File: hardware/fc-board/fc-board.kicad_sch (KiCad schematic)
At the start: 0 parts

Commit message: Add hierarchical sheet structure: power, MCU, IMU, motors, radio
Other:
- added sheet IMU (imu.kicad_sch)
- added sheet MCU (mcu.kicad_sch)
- added sheet Motors (motors.kicad_sch)
- added sheet Power (power.kicad_sch)
- added sheet Radio (radio.kicad_sch)
- company: (none) -> Brody Barrett
- title: (none) -> STM32 Quadcopter Flight Controller
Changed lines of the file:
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@@
 	(generator_version "10.0")
 	(paper "A4")
+	(title_block
+		(title "STM32 Quadcopter Flight Controller")
+		(company "Brody Barrett")
+		(comment 1 "Rev A")
+		(comment 2 "github.com/barrettbrody06/stm32-quadcopter-fc")
+	)
+	(sheet
+		(at 190.5 16.51)
+		(size 87.63 62.23)
+		(exclude_from_sim no)
+		(in_bom yes)
+		(on_board yes)
+		(dnp no)
+		(fields_autoplaced yes)
+		(stroke
+			(width 0.1524)
+			(type solid)
+		)
+		(fill
+			(color 0 0 0 0)
+		)
+		(property "Sheetname" "Radio"
+			(at 190.5 15.7984 0)
+			(show_name no)
+			(do_not_autoplace no)
+			(effects
+				(font
+					(size 1.27 1.27)
+				)
+				(justify left bottom)
+			)
+		)
+		(property "Sheetfile" "radio.kicad_sch"
+			(at 190.5 79.3246 0)
+			(show_name no)
+			(do_not_autoplace no)
+			(effects
+				(font
+					(size 1.27 1.27)
+				)
+				(justify left top)
+			)
+		)
+		(instances
+			(project "fc-board"
+				(path "/953cb3c2-4b9e-42b9-907c-fb15c6a3ba2f"
+					(page "6")
+				)
+			)
+		)
+	)
+	(sheet
+		(at 97.79 16.51)
+		(size 86.36 109.22)
+		(exclude_from_sim no)
+		(in_bom yes)
+		(on_board yes)
+		(dnp no)
+		(fields_autoplaced yes)
+		(stroke
+			(width 0.1524)
+			(type solid)
+		)
+		(fill
+			(color 0 0 0 0)
+		)
+		(property "Sheetname" "MCU"
+			(at 97.79 15.7984 0)
+			(show_name no)
+			(do_not_autoplace no)
+			(effects
+				(font
+					(size 1.27 1.27)
+				)
+				(justify left bottom)
+			)
+		)
+		(property "Sheetfile" "mcu.kicad_sch"
+			(at 97.79 126.3146 0)
+			(show_name no)
+			(do_not_autoplace no)
+			(effects
+				(font
+					(size 1.27 1.27)
+				)
+				(justify left top)
+			)
+		)
+		(instances
+			(project "fc-board"
+				(path "/953cb3c2-4b9e-42b9-907c-fb15c6a3ba2f"
+					(page "3")
+				)
+			)
+		)
+	)
+	(sheet
+		(at 15.24 16.51)
+		(size 74.93 40.64)
+		(exclude_from_sim no)
+		(in_bom yes)
+		(on_board yes)
+		(dnp no)
+		(fields_autoplaced yes)
+		(stroke
+			(width 0.1524)
+			(type solid)
+		)
+		(fill
+			(color 0 0 0 0)
+		)
+		(property "Sheetname" "Power"
+			(at 15.24 15.7984 0)
+			(show_name no)
+			(do_not_autoplace no)
+			(effects
+				(font
+					(size 1.27 1.27)
+				)
+				(justify left bottom)
+			)
+		)
+		(property "Sheetfile" "power.kicad_sch"
+			(at 15.24 57.7346 0)
+			(show_name no)
+			(do_not_autoplace no)
+			(effects
+				(font
+					(size 1.27 1.27)
+				)
+				(justify left top)
+			)
+		)
+		(instances
+			(project "fc-board"
+				(path "/953cb3c2-4b9e-42b9-907c-fb15c6a3ba2f"
+					(page "2")
+				)
+			)
+		)
+	)
+	(sheet
+		(at 83.82 132.08)
+		(size 90.17 63.5)
+		(exclude_from_sim no)
+		(in_bom yes)
+		(on_board yes)
+		(dnp no)
+		(fields_autoplaced yes)
+		(stroke
+			(width 0.1524)
+			(type solid)
+		)
+		(fill
+			(color 0 0 0 0)
+		)
+		(property "Sheetname" "Motors"
+			(at 83.82 131.3684 0)
+			(show_name no)
+			(do_not_autoplace no)
+			(effects
+				(font
+					(size 1.27 1.27)
+				)
+				(justify left bottom)
+			)
+		)
+		(property "Sheetfile" "motors.kicad_sch"
+			(at 83.82 196.1646 0)
+			(show_name no)
+			(do_not_autoplace no)
+			(effects
+				(font
+					(size 1.27 1.27)
+				)
+				(justify left top)
+			)
+		)
+		(instances
+			(project "fc-board"
+				(path "/953cb3c2-4b9e-42b9-907c-fb15c6a3ba2f"
+					(page "5")
+				)
+			)
+		)
+	)
+	(sheet
+		(at 15.24 68.58)
+		(size 74.93 57.15)
+		(exclude_from_sim no)
+		(in_bom yes)
+		(on_board yes)
+		(dnp no)
+		(fields_autoplaced yes)
+		(stroke
+			(width 0.1524)
+			(type solid)
+		)
+		(fill
+			(color 0 0 0 0)
+		)
+		(property "Sheetname" "IMU"
+			(at 15.24 67.8684 0)
+			(show_name no)
+			(do_not_autoplace no)
+			(effects
+				(font
+					(size 1.27 1.27)
+				)
+				(justify left bottom)
+			)
+		)
+		(property "Sheetfile" "imu.kicad_sch"
+			(at 15.24 126.3146 0)
+			(show_name no)
+			(do_not_autoplace no)
+			(effects
+				(font
+					(size 1.27 1.27)
+				)
+				(justify left top)
+			)
+		)
+		(instances
+			(project "fc-board"
+				(path "/953cb3c2-4b9e-42b9-907c-fb15c6a3ba2f"
+					(page "4")
+				)
+			)
+		)
+	)
 	(sheet_instances
 		(path "/"

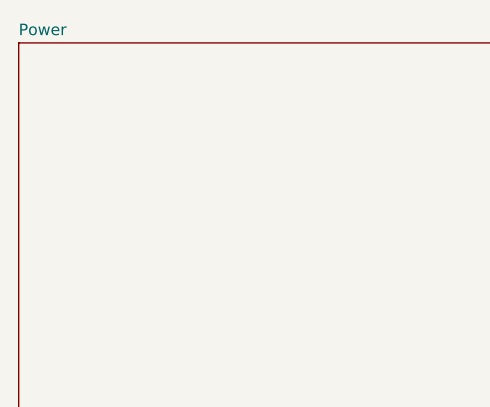
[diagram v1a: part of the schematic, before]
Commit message: Power sheet complete: PWR_FLAGs, no-connect on EN, ERC clean
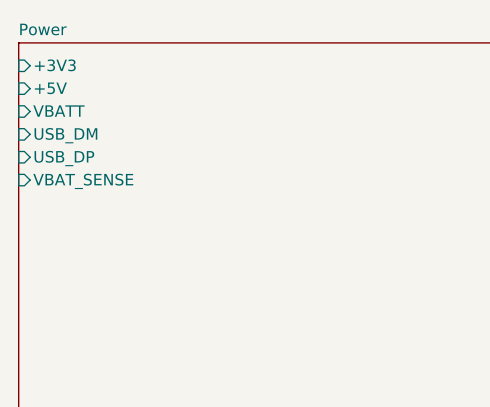
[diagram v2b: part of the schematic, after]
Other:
- sheet Power ports: added +3V3, +5V, USB_DM, USB_DP, VBATT, VBAT_SENSE; removed none
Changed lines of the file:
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@@
+			)
+		)
+		(pin "+3V3" input
+			(at 15.24 19.05 180)
+			(effects
+				(font
+					(size 1.27 1.27)
+				)
+				(justify left)
+			)
+		)
+		(pin "+5V" input
+			(at 15.24 21.59 180)
+			(effects
+				(font
+					(size 1.27 1.27)
+				)
+				(justify left)
+			)
+		)
+		(pin "USB_DM" input
+			(at 15.24 26.67 180)
+			(effects
+				(font
+					(size 1.27 1.27)
+				)
+				(justify left)
+			)
+		)
+		(pin "USB_DP" input
+			(at 15.24 29.21 180)
+			(effects
+				(font
+					(size 1.27 1.27)
+				)
+				(justify left)
+			)
+		)
+		(pin "VBATT" input
+			(at 15.24 24.13 180)
+			(effects
+				(font
+					(size 1.27 1.27)
+				)
+				(justify left)
+			)
+		)
+		(pin "VBAT_SENSE" input
+			(at 15.24 31.75 180)
+			(effects
+				(font
+					(size 1.27 1.27)
+				)
+				(justify left)
 			)
 		)

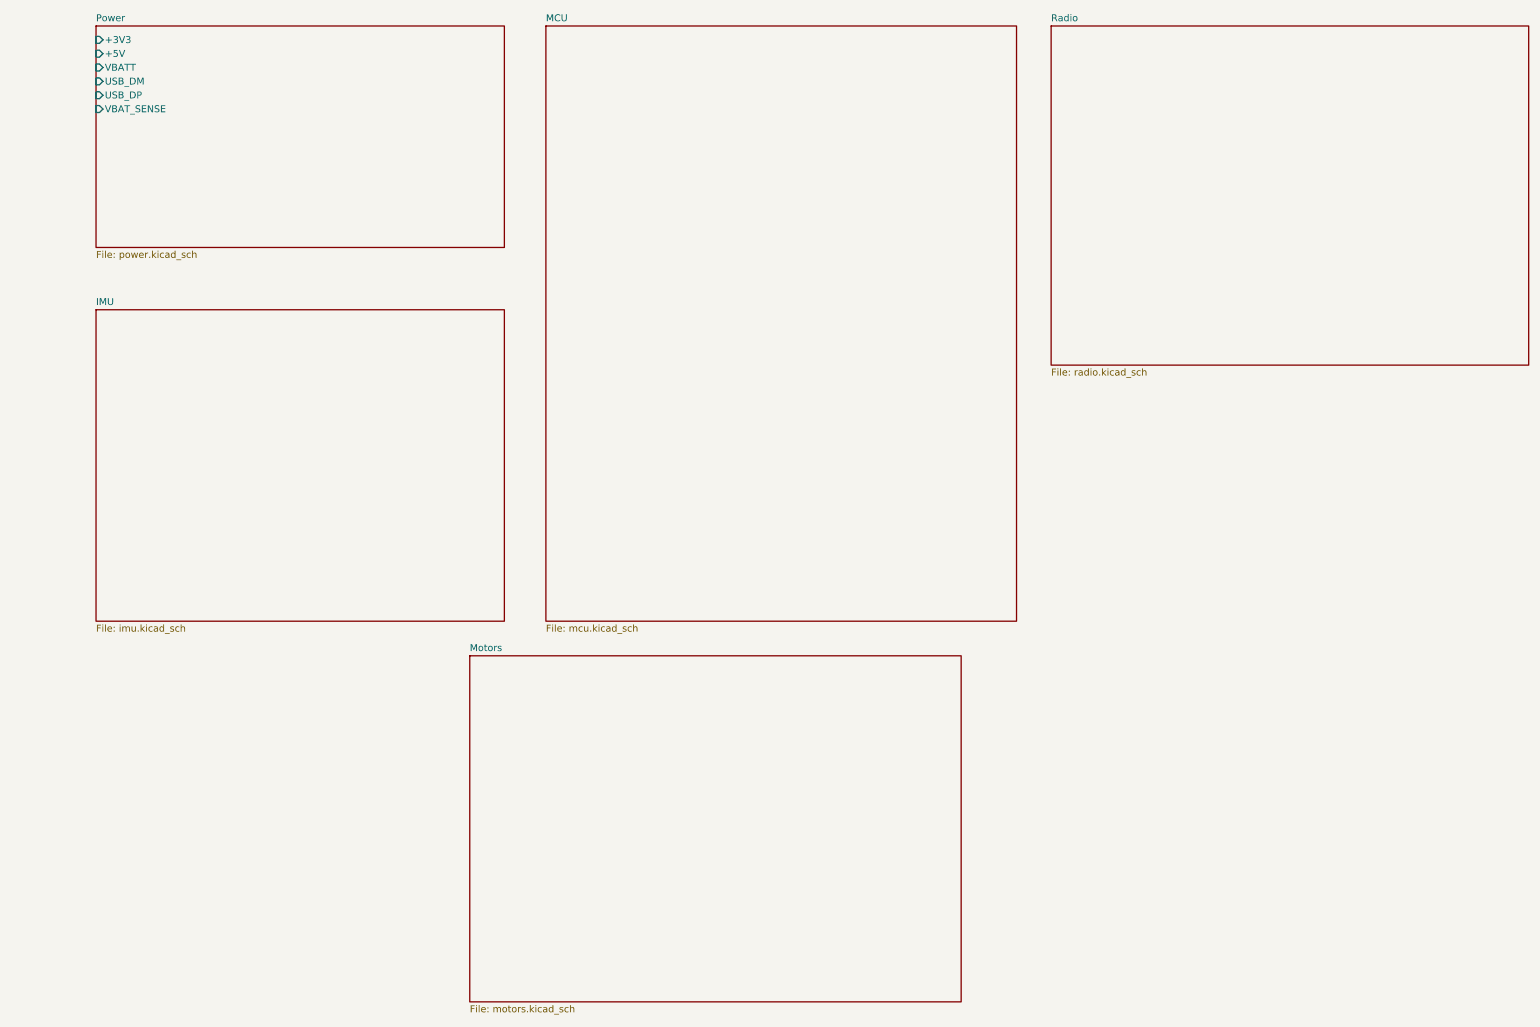
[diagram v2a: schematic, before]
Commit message: MCU sheet: F411 core, HSE, SWD, boot select; ERC fixes
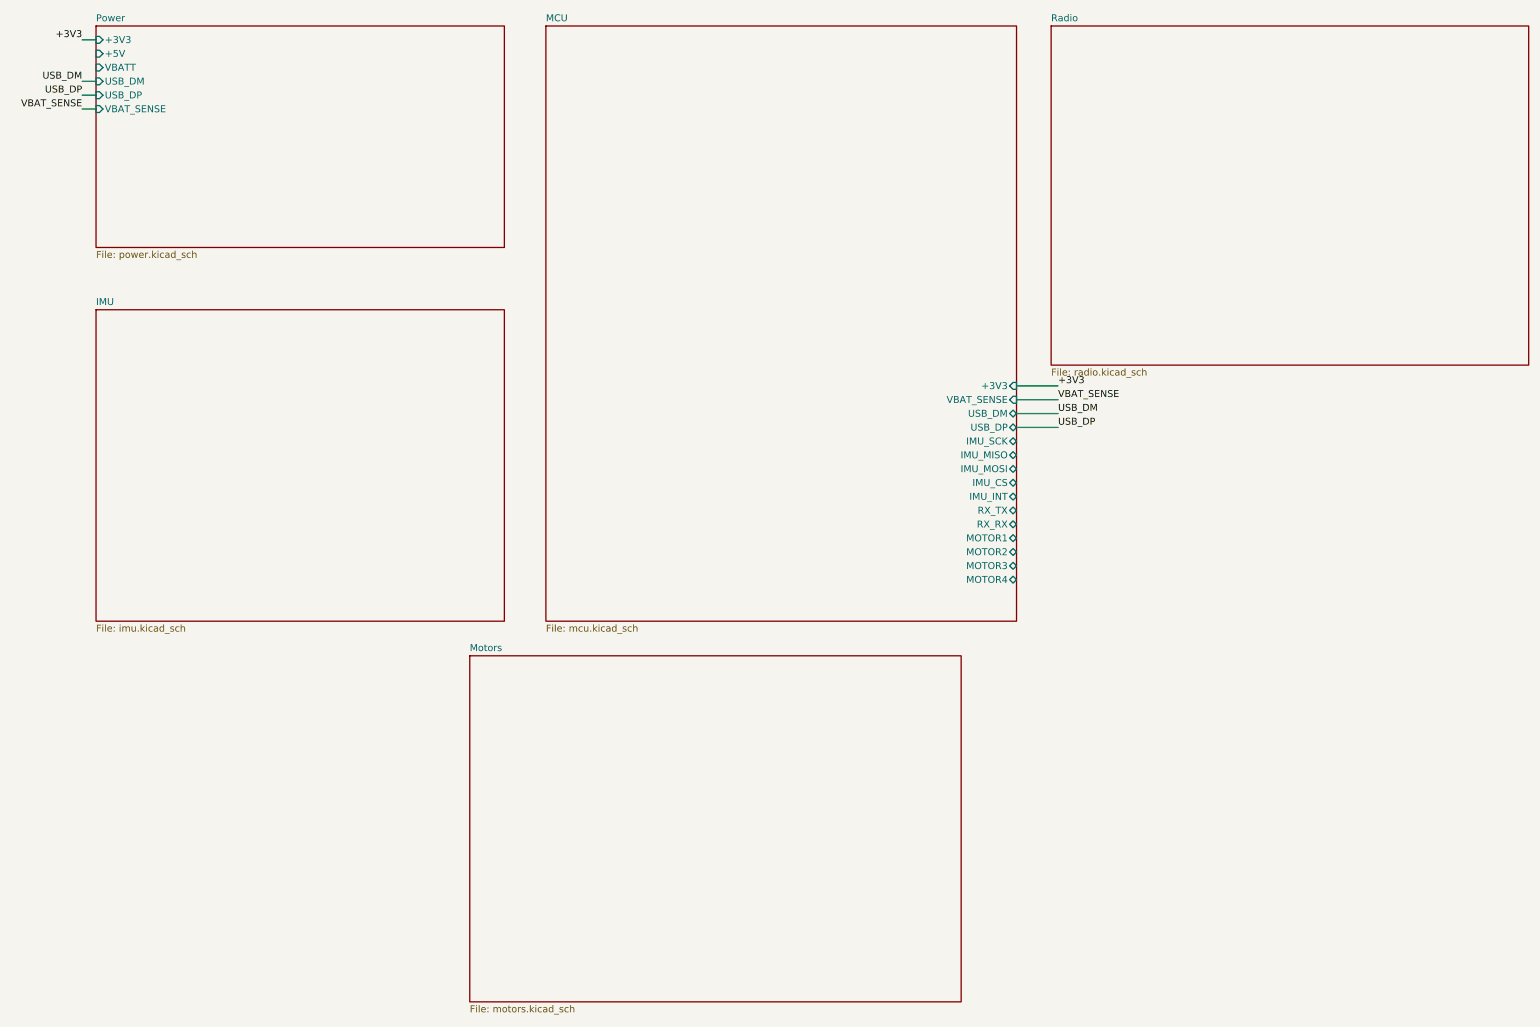
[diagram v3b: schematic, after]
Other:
- sheet MCU ports: added +3V3, IMU_CS, IMU_INT, IMU_MISO, IMU_MOSI, IMU_SCK, MOTOR1, MOTOR2, MOTOR3, MOTOR4, RX_RX, RX_TX, USB_DM, USB_DP, VBAT_SENSE; removed none

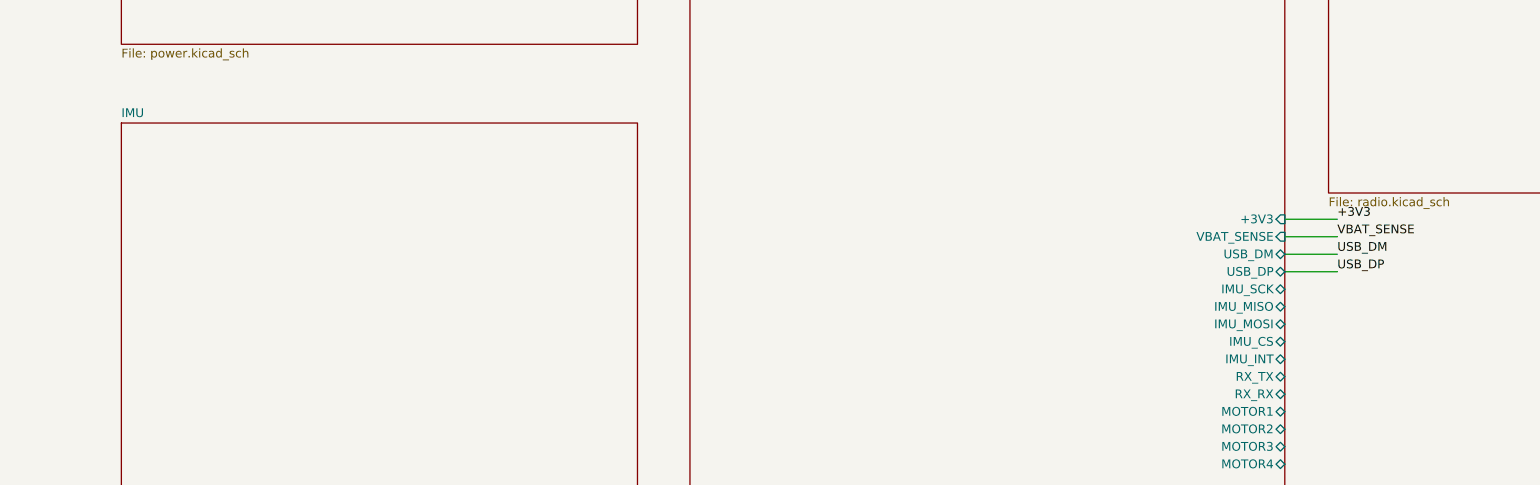
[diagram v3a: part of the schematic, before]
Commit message: IMU sheet: ICM-42605 on SPI1
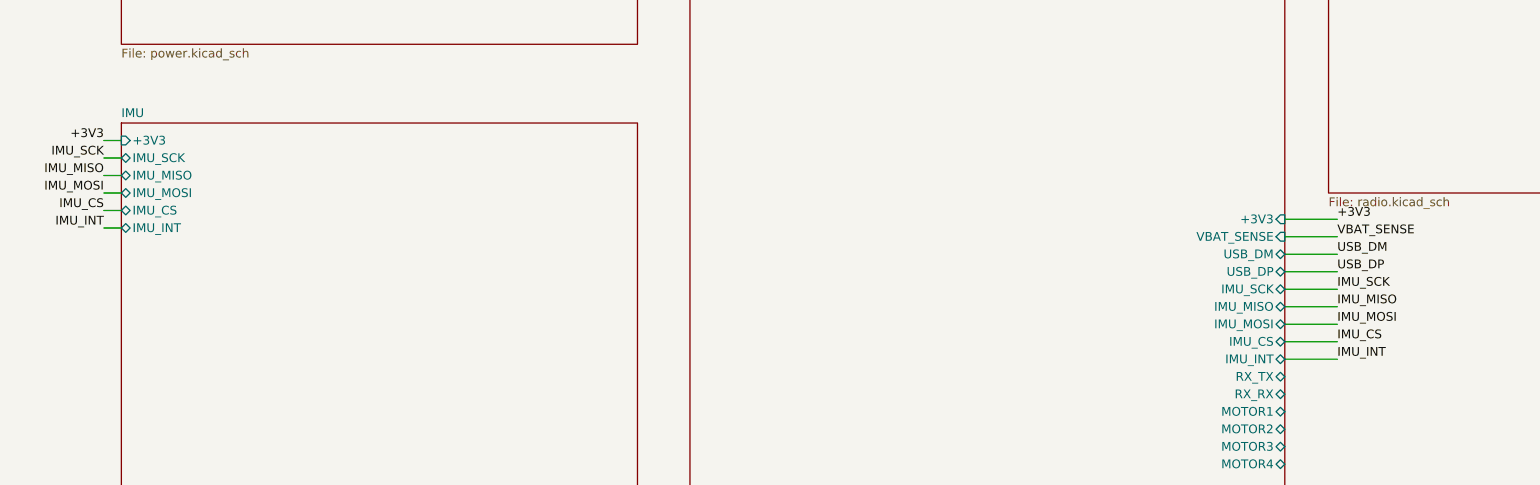
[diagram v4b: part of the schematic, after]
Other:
- sheet IMU ports: added +3V3, IMU_CS, IMU_INT, IMU_MISO, IMU_MOSI, IMU_SCK; removed none

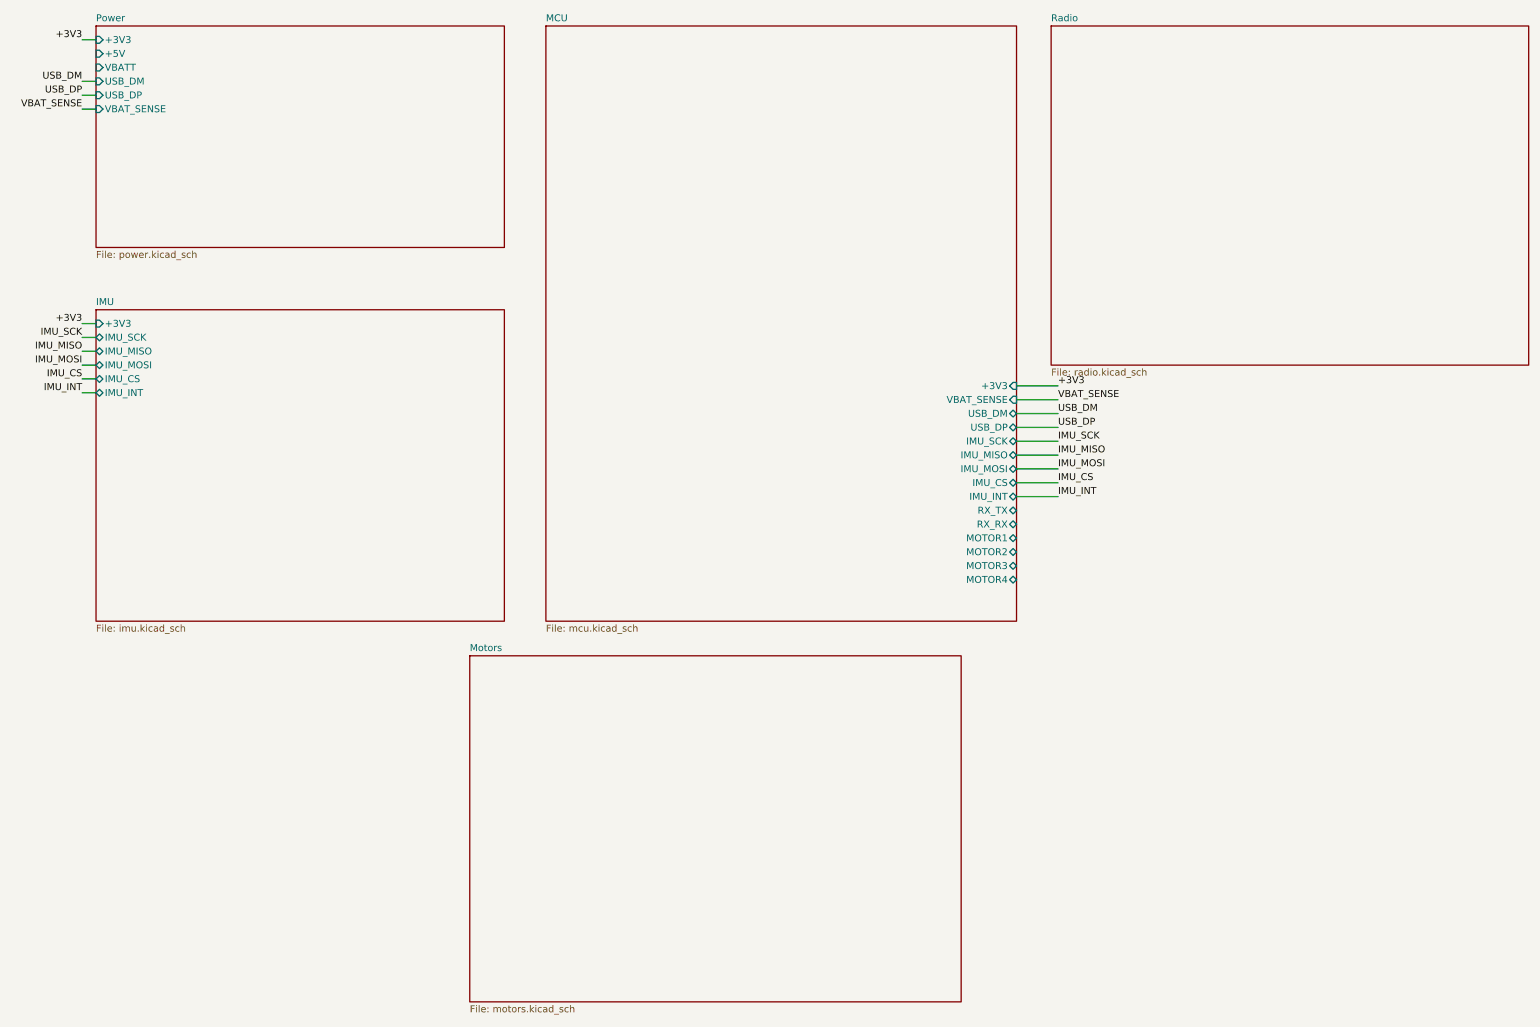
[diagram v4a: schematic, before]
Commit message: IMU, Motors, Radio sheets; schematic complete
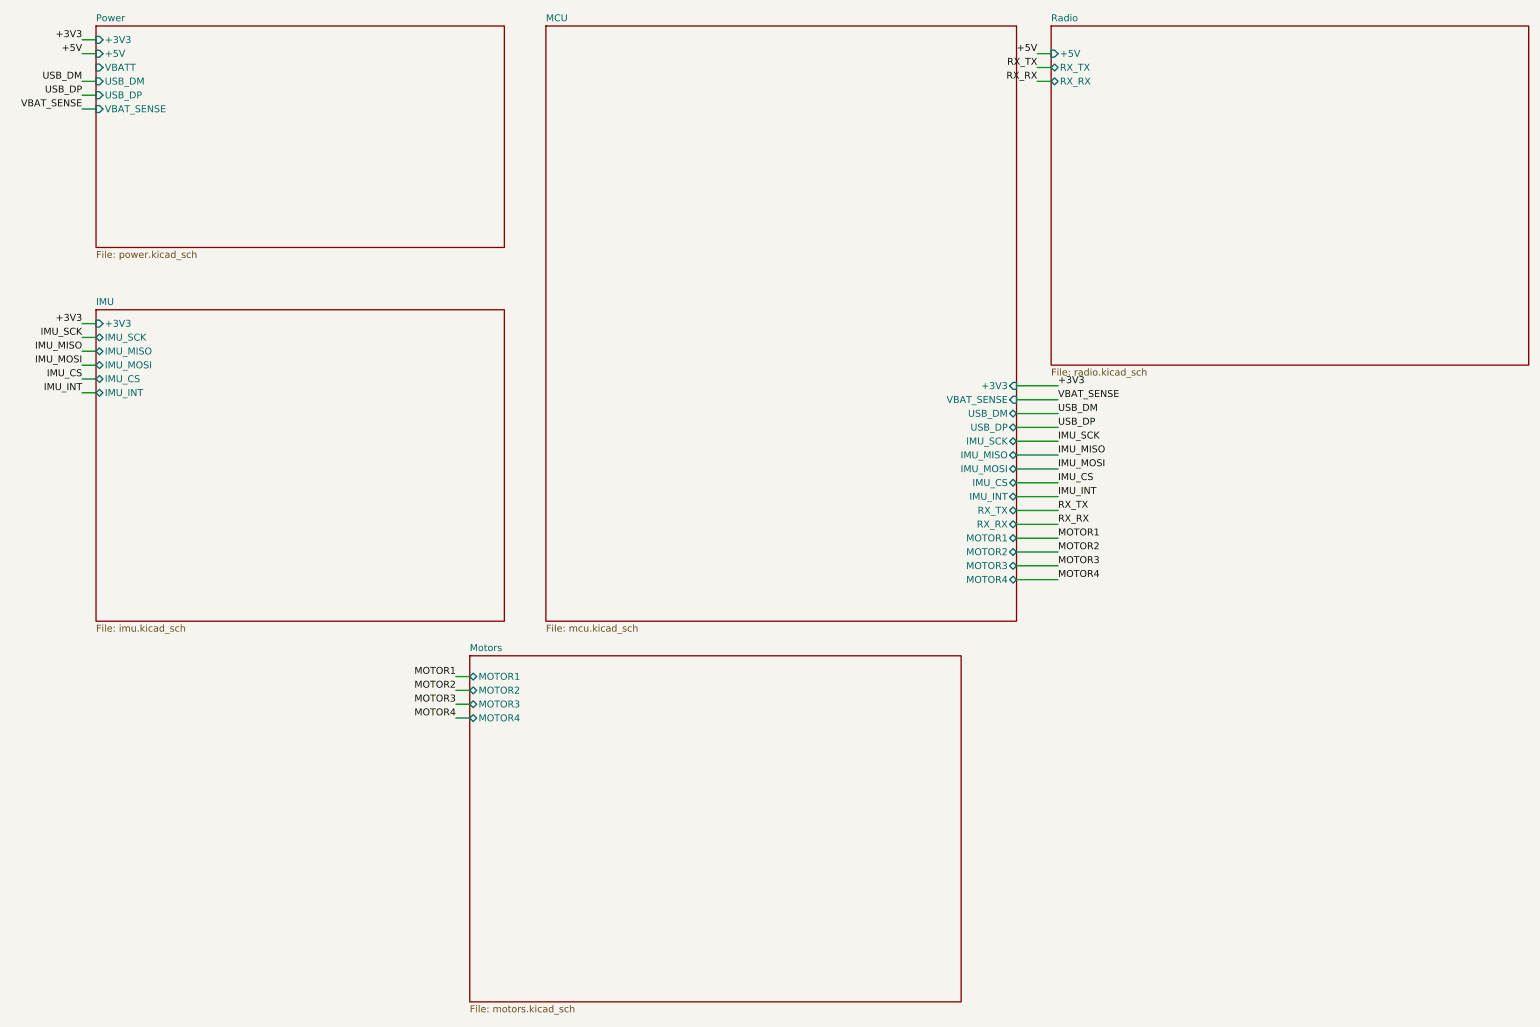
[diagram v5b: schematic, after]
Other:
- sheet Motors ports: added MOTOR1, MOTOR2, MOTOR3, MOTOR4; removed none
- sheet Radio ports: added +5V, RX_RX, RX_TX; removed none
